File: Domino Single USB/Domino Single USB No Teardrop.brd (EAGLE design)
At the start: 25.4 x 33 mm, 22 parts, among them J1 MH10-1, J2 USB_AF-006, J3 MH10-1

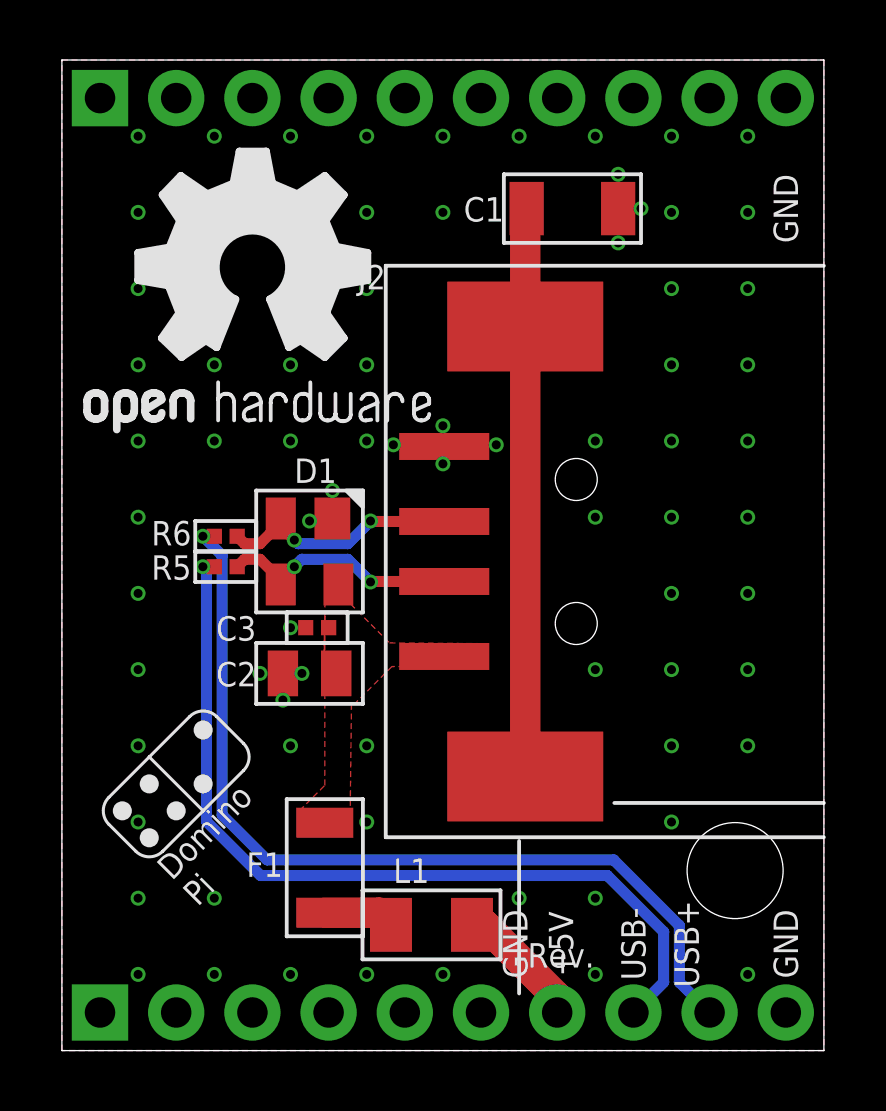
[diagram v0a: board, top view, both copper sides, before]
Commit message: Re-routed Single USB tile to remove vias on USB traces
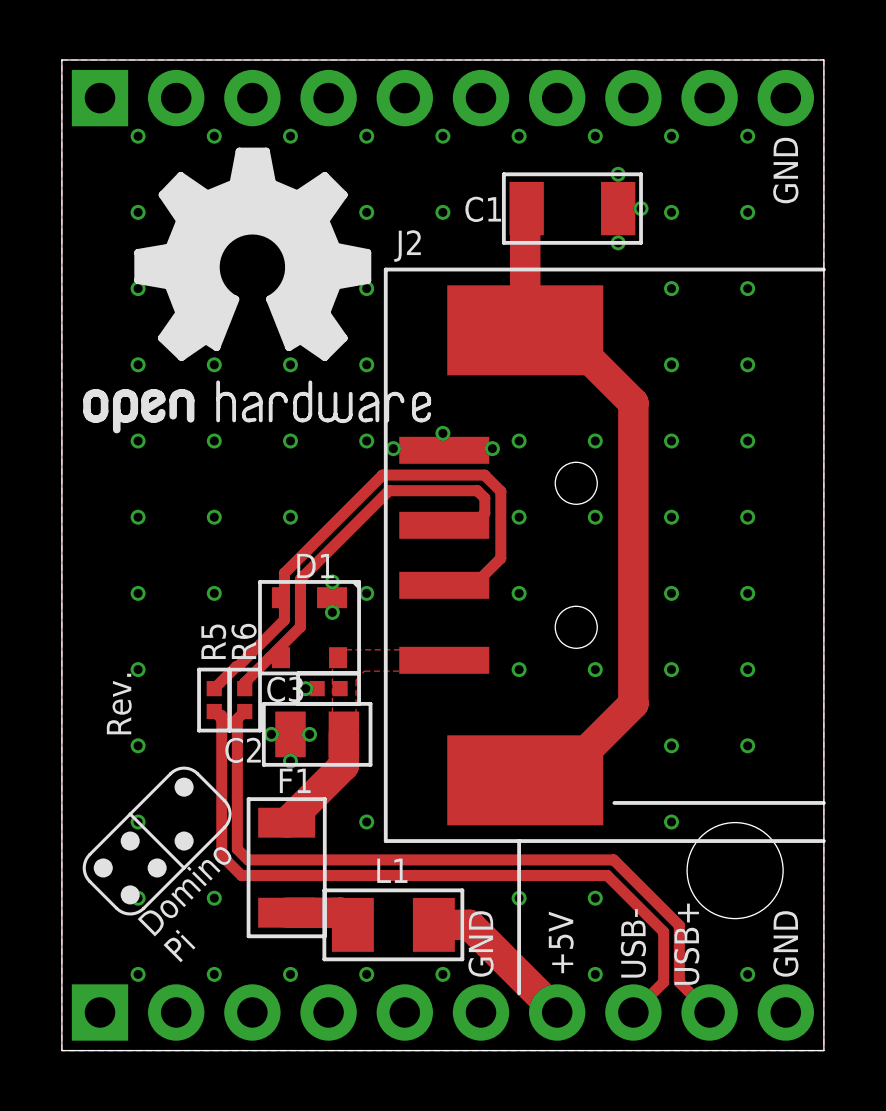
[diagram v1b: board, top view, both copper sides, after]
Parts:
- moved R6 5.50 mm to (6.10, 11.7), turned to 270 degrees
- moved R5 4.46 mm to (5.08, 11.7), turned to 270 degrees
- moved D1 2.54 mm to (8.26, 14.1)
- moved C3 2.07 mm to (8.89, 12.1)
- moved C2 2.05 mm to (8.51, 10.5)
- moved U$10 2.01 mm to (3.17, 6.99)
- moved L1 1.27 mm to (11.0, 4.19)
- moved F1 1.27 mm to (7.49, 6.10)
- moved J2 0.13 mm to (17.1, 16.5)
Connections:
- net D_N: now also D1.2; no longer D1.3
- net D_P: now also D1.3; no longer D1.2
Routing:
- net D_N: track 8.19 -> 18.3 mm, vias 2 -> 0
- net USB_P: track 30.0 -> 23.8 mm, vias 1 -> 0
- net D_P: track 8.07 -> 14.3 mm, vias 2 -> 0
- net USB_N: track 28.8 -> 23.9 mm, vias 1 -> 0
- net PE: track 19.0 -> 23.5 mm
- net VBUS: track 0.00 -> 3.73 mm
- net +5V: track 4.35 -> 5.32 mm

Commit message: Domino Single USB Rev. C: changed Logos
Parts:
- removed U$13: (no value), Domino:OPEN_HARDWARE_LOGO
- added U$7: DOMINO_LOGO, Domino:DOMINO_LOGO
- moved U$11 11.4 mm to (14.0, 6.35)
- moved U$10 10.8 mm to (3.81, 17.8), turned to 90 degrees
- moved U$4 9.52 mm to (22.9, 16.5)
- moved U$8 1.27 mm to (5.71, 3.81)
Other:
- board text removed: "Domino Core"
- board text removed: "Domino Pi"
- board text removed: "Domino Qi"

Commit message: Domino Single USB Rev. C: removed the resetable fuse that causes too much drop for high-current USB devices
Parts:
- removed F1: 0ZCA0050FF2G, Domino:PTC1206
- moved L1 2.52 mm to (9.40, 6.10), turned to 90 degrees
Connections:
- removed net VPROT: F1.1, L1.2
- net VBUS: now also L1.2; no longer F1.2
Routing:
- net +5V: track 5.32 -> 8.55 mm
- net VPROT: track 2.37 -> 0.00 mm
- net VBUS: track 3.73 -> 3.10 mm
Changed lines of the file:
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@@
 <layer number="143" name="mvRestrict" color="7" fill="1" visible="no" active="no"/>
 <layer number="144" name="DrillLegend" color="7" fill="1" visible="yes" active="yes"/>
-<layer number="145" name="DrillLegend_01-16" color="2" fill="9" visible="no" active="yes"/>
-<layer number="146" name="DrillLegend_01-20" color="3" fill="9" visible="no" active="yes"/>
+<layer number="145" name="DrillLegend_01-16" color="2" fill="9" visible="yes" active="yes"/>
+<layer number="146" name="DrillLegend_01-20" color="3" fill="9" visible="yes" active="yes"/>
 <layer number="147" name="mMeasures" color="7" fill="1" visible="no" active="no"/>
 <layer number="148" name="mDocument" color="7" fill="1" visible="no" active="no"/>
@@
 <wire x1="20.32" y1="8.128" x2="20.32" y2="7.112" width="0.1016" layer="145"/>
 <wire x1="19.812" y1="7.62" x2="20.828" y2="7.62" width="0.1016" layer="145"/>
-<wire x1="10.16" y1="8.128" x2="10.16" y2="7.112" width="0.1016" layer="145"/>
-<wire x1="9.652" y1="7.62" x2="10.668" y2="7.62" width="0.1016" layer="145"/>
+<wire x1="10.795" y1="8.128" x2="10.795" y2="7.112" width="0.1016" layer="145"/>
+<wire x1="10.287" y1="7.62" x2="11.303" y2="7.62" width="0.1016" layer="145"/>
 <wire x1="2.54" y1="8.128" x2="2.54" y2="7.112" width="0.1016" layer="145"/>
 <wire x1="2.032" y1="7.62" x2="3.048" y2="7.62" width="0.1016" layer="145"/>
@@
 </plain>
 <attributes>
-<attribute name="DATE" value="20141230"/>
+<attribute name="DATE" value="20141231"/>
 <attribute name="DRAWN" value="M.STEMPIN"/>
 <attribute name="REV" value="C"/>
@@
 <attribute name="VALUE" x="8.89" y="12.065" size="0.8128" layer="27" rot="R180" align="center"/>
 </element>
-<element name="L1" library="Domino" package="FB1206" value="BLM31PG601SN1L" x="11.049" y="4.191" smashed="yes" rot="R180">
-<attribute name="SIZE" value="1206" x="30.099" y="-9.779" size="1.27" layer="27" rot="R180" display="off"/>
-<attribute name="PARTNO" value="BLM31PG601SN1L" x="30.099" y="-9.779" size="1.27" layer="27" rot="R180" display="off"/>
-<attribute name="OPT" value="600R/1A5" x="30.099" y="-9.779" size="1.27" layer="27" rot="R180" display="off"/>
-<attribute name="NAME" x="10.414" y="5.588" size="0.8128" layer="25" ratio="12"/>
-<attribute name="VALUE" x="11.049" y="4.191" size="0.8128" layer="27" ratio="12" rot="R180" align="center"/>
+<element name="L1" library="Domino" package="FB1206" value="BLM31PG601SN1L" x="9.398" y="6.096" smashed="yes" rot="R90">
+<attribute name="SIZE" value="1206" x="-4.572" y="-12.954" size="1.27" layer="27" rot="R90" display="off"/>
+<attribute name="PARTNO" value="BLM31PG601SN1L" x="-4.572" y="-12.954" size="1.27" layer="27" rot="R90" display="off"/>
+<attribute name="OPT" value="600R/1A5" x="-4.572" y="-12.954" size="1.27" layer="27" rot="R90" display="off"/>
+<attribute name="NAME" x="10.668" y="5.588" size="0.8128" layer="25" ratio="12"/>
+<attribute name="VALUE" x="9.398" y="6.096" size="0.8128" layer="27" ratio="12" rot="R90" align="center"/>
 </element>
 <element name="C2" library="Domino" package="C0805" value="10u" x="8.509" y="10.541" smashed="yes" rot="R180">
@@
 <attribute name="VALUE" x="8.509" y="10.541" size="0.8128" layer="27" rot="R180" align="center"/>
 </element>
-<element name="F1" library="Domino" package="PTC1206" value="0ZCA0050FF2G" x="7.493" y="6.096" smashed="yes" rot="R90">
-<attribute name="PARTNO" value="0ZCG0110FF2C" x="7.493" y="-11.684" size="1.27" layer="27" rot="R90" display="off"/>
-<attribute name="VOLT" value="8V" x="7.493" y="6.096" size="1.778" layer="27" rot="R90" display="off"/>
-<attribute name="RATE" value="0.5A" x="7.493" y="6.096" size="1.778" layer="27" rot="R90" display="off"/>
-<attribute name="NAME" x="8.382" y="9.398" size="0.8128" layer="25" rot="R180"/>
-<attribute name="VALUE" x="7.493" y="6.096" size="0.8128" layer="27" rot="R90" align="center"/>
-</element>
 <element name="J2" library="Domino" package="USB_AF-006" value="USB_AF-006" x="17.145" y="16.51" smashed="yes" rot="R90">
 <attribute name="PARTNO" value="USB_AF-006" x="17.145" y="16.51" size="1.778" layer="27" rot="R90" display="off"/>
@@
 <element name="U$1" library="Domino" package="ROHS_LOGO" value="" x="22.86" y="21.59" rot="MR0"/>
 <element name="U$11" library="Domino" package="ESD_LOGO" value="" x="13.97" y="6.35" rot="MR0"/>
-<element name="DRILEGEND" library="drilegend" package="DRILEGEND" value="" x="81.534" y="59.944"/>
 <element name="U$7" library="Domino" package="DOMINO_LOGO" value="DOMINO_LOGO" x="-45.72" y="-48.26">
 <attribute name="BOM" value="EXCLUDE" x="-45.72" y="-48.26" size="1.27" layer="27" display="off"/>
@@
 <element name="U$4" library="Domino" package="DOMINO_LOGO_SMALL" value="" x="22.86" y="16.51" rot="MR0"/>
 <element name="U$10" library="Domino" package="DOMINO_LOGO_SMALL" value="" x="3.81" y="17.78" rot="R90"/>
+<element name="DRILEGEND" library="drilegend" package="DRILEGEND" value="" x="81.534" y="59.944"/>
 </elements>
 <signals>
@@
 <via x="22.86" y="10.16" extent="1-16" drill="0.3"/>
 <via x="20.32" y="7.62" extent="1-16" drill="0.3"/>
-<via x="10.16" y="7.62" extent="1-16" drill="0.3"/>
+<via x="10.795" y="7.62" extent="1-16" drill="0.3"/>
 <via x="2.54" y="7.62" extent="1-16" drill="0.3"/>
 <via x="2.54" y="5.08" extent="1-16" drill="0.3"/>
@@
 <contactref element="C2" pad="1"/>
 <contactref element="C3" pad="1"/>
-<contactref element="F1" pad="2"/>
 <contactref element="J2" pad="1"/>
-<wire x1="9.398" y1="10.541" x2="9.398" y2="9.501" width="1.016" layer="1"/>
-<wire x1="9.398" y1="9.501" x2="7.493" y2="7.596" width="1.016" layer="1"/>
 <polygon width="0.2032" layer="1" thermals="no">
 <vertex x="14.1478" y="13.3604"/>
@@
 <vertex x="14.1478" y="12.6492"/>
 </polygon>
+<contactref element="L1" pad="2"/>
+<wire x1="9.398" y1="10.541" x2="9.398" y2="7.446" width="1.016" layer="1"/>
 </signal>
 <signal name="PE">
@@
 <wire x1="15.445" y1="9.01" x2="16.503" y2="9.01" width="1.016" layer="1"/>
 </signal>
-<signal name="VPROT">
-<contactref element="L1" pad="2"/>
-<contactref element="F1" pad="1"/>
-<wire x1="7.493" y1="4.596" x2="9.294" y2="4.596" width="1.016" layer="1"/>
-<wire x1="9.294" y1="4.596" x2="9.699" y2="4.191" width="1.016" layer="1"/>
-</signal>
 <signal name="+5V">
 <contactref element="L1" pad="1"/>
 <contactref element="J1" pad="7"/>
-<wire x1="12.399" y1="4.191" x2="13.589" y2="4.191" width="1.016" layer="1"/>
 <wire x1="13.589" y1="4.191" x2="16.51" y2="1.27" width="1.016" layer="1"/>
+<wire x1="13.589" y1="4.191" x2="9.953" y2="4.191" width="1.016" layer="1"/>
+<wire x1="9.953" y1="4.191" x2="9.398" y2="4.746" width="1.016" layer="1"/>
 </signal>
 <signal name="USB_P" class="1">

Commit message: Added USB power switch to Sinfle USB tile
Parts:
- added C4: 10u, Domino:C0805
- added C5: 1n, Domino:C1206
- added R1: 100k, Domino:R0402
- added R2: 15k, Domino:R0402
- added U1: MP65151DJ, Domino:SOT23-6
- C1: value 1n -> 10u; device Domino:C1206 -> Domino:C0603
- C2: value 10u -> 220u; device Domino:C0805 -> Domino:C/6032-25
- J2: value USB_AF-006 -> MH10-1; device Domino:USB_AF-006 -> Domino:MH10-1-0.1
- J3: value MH10-1 -> USB_AF-006; device Domino:MH10-1-0.1 -> Domino:USB_AF-006
- moved J1 30.5 mm to (1.27, 31.8)
- moved J2 22.0 mm to (1.27, 1.27), flipped to the bottom, turned to 180 degrees
- moved J3 22.0 mm to (17.1, 16.5), flipped to the top, turned to 90 degrees
- moved C1 21.1 mm to (3.30, 12.1), turned to 180 degrees
- moved C2 7.41 mm to (2.16, 6.73), turned to 270 degrees
- moved U$10 1.17 mm to (2.67, 18.0)
- renumbered R5 to R3, R6 to R4, U$7 to S1
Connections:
- new net DP_PWR: C2.1, L1.1, U1.6
- new net ILIM: R2.1, U1.5
- new net JTAG_TDI: J1.3, R1.1, U1.3
- net +5V: now also C1.1, J2.7, R1.2, U1.1; no longer J1.7, L1.1
- net D_N: now also J3.2; no longer J2.2
- net D_P: now also J3.3; no longer J2.3
- net GND: now also C4.2, C5.2, J2.10, J2.6, J3.4, R2.2, U1.2; no longer J1.6, J2.4, J3.10
- net PE: now also C5.1, J3.S$1, J3.S$2; no longer C1.1, J2.S$1, J2.S$2
- net USB_N: now also J2.8; no longer J1.8
- net USB_P: now also J2.9; no longer J1.9
- net VBUS: now also C4.1, J3.1; no longer C2.1, J2.1
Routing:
- net +5V: track 8.55 -> 28.2 mm, vias 0 -> 2
- net JTAG_TDI: track 0.00 -> 17.3 mm
- net DP_PWR: track 0.00 -> 16.5 mm
- net ILIM: track 0.00 -> 3.44 mm
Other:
- board text added: "JTAG_TDI"
- board text added: "© 2014-2015, The Domino Team. All rights reserved."
- board text removed: "© 2014, The Domino Team. All rights reserved."

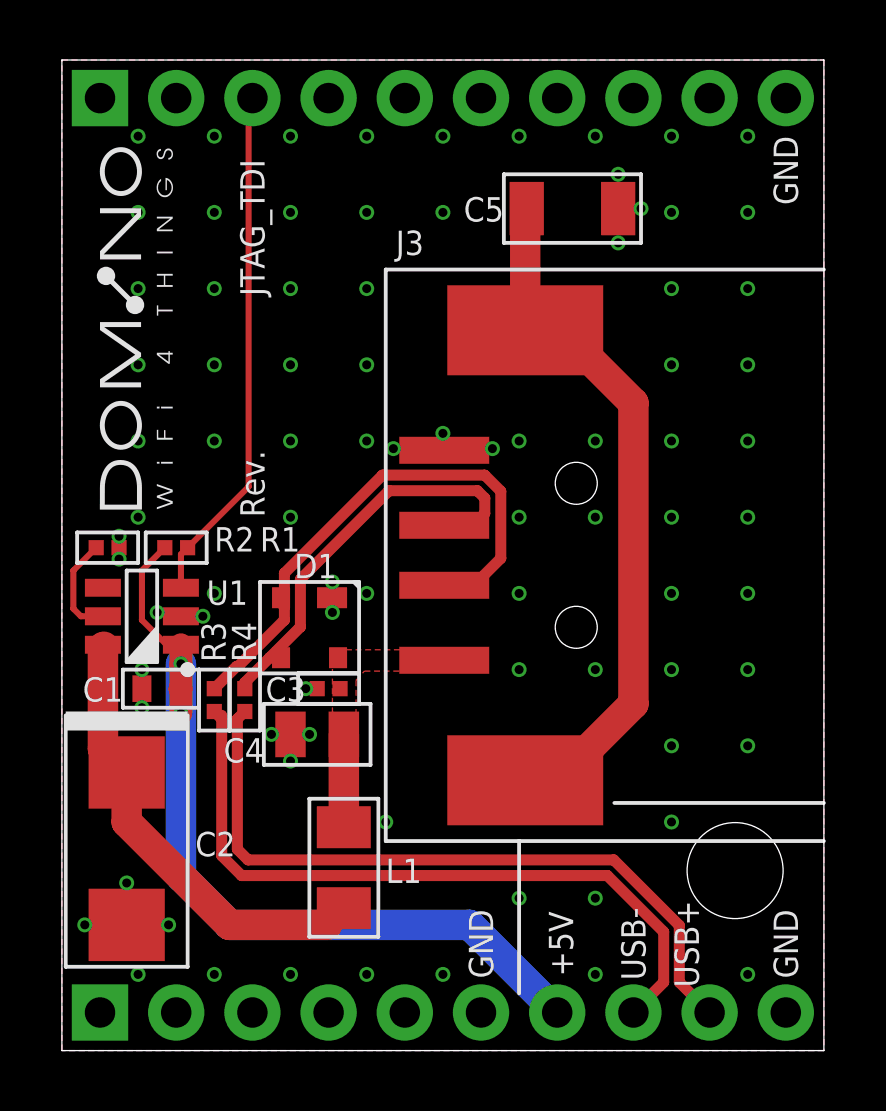
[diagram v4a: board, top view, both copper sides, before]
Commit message: Domino Single USB tile Rev. D: added resistors en power siwtch feedback and enable, changed output capacitor to smaller one
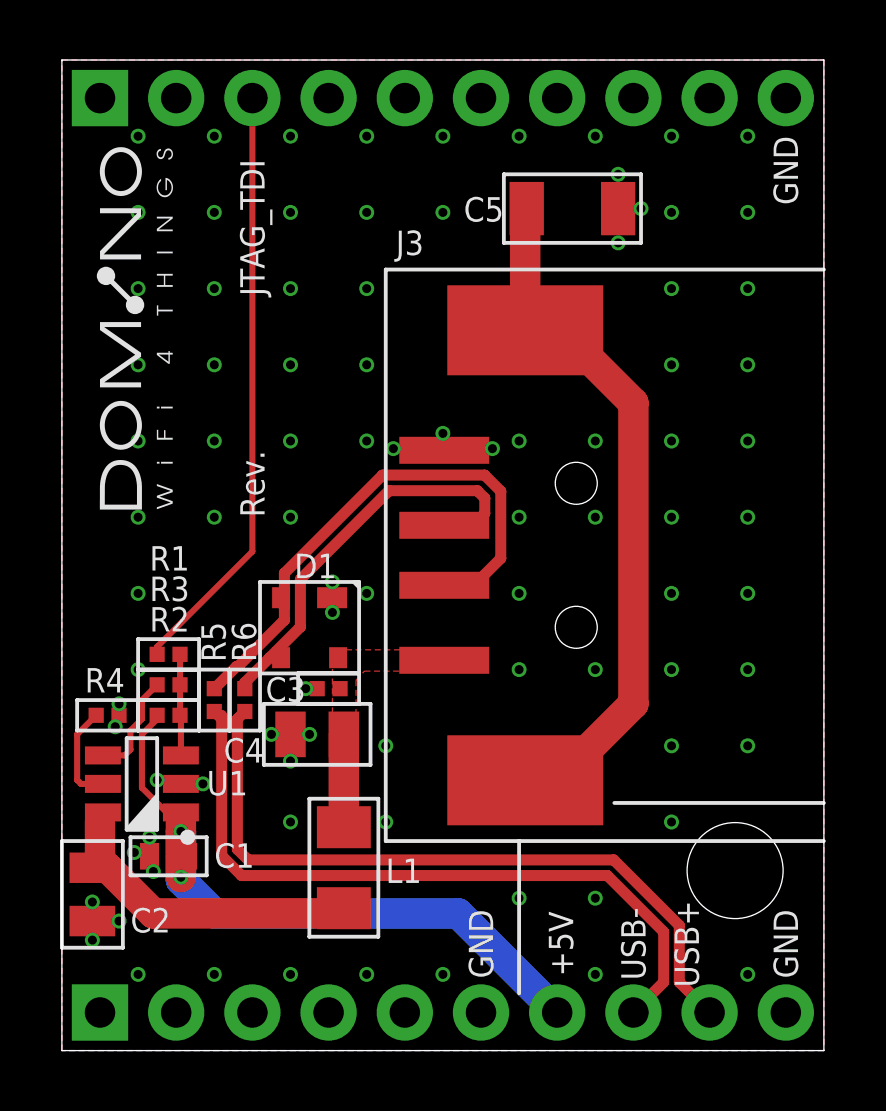
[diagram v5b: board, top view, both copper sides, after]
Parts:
- added R5, R6: 0R, Domino:R0402
- C2: value 220u -> 22u; device Domino:C/6032-25 -> Domino:C0805
- R1: value 100k -> 33R
- R2: value 15k -> 100k
- R4: value 0R -> 15k
- moved R2 5.95 mm to (3.56, 11.2), turned to 180 degrees
- moved C1 5.59 mm to (3.56, 6.48)
- moved U1 5.59 mm to (2.67, 8.89)
- moved R4 4.60 mm to (1.52, 11.2), turned to 0 degrees
- moved R1 3.57 mm to (3.56, 13.2)
- moved C2 1.91 mm to (1.02, 5.21)
- moved R3 1.61 mm to (3.56, 12.2), turned to 0 degrees
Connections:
- new net EN: R1.1, R2.1, R3.2, U1.3
- new net N$1: R3.1, U1.4
- net +5V: now also R2.2; no longer R1.2
- net D_N: now also R5.1; no longer R3.1
- net D_P: now also R6.1; no longer R4.1
- net GND: now also R4.2; no longer R2.2
- net ILIM: now also R4.1; no longer R2.1
- net JTAG_TDI: now also R1.2; no longer R1.1, U1.3
- net USB_N: now also R5.2; no longer R3.2
- net USB_P: now also R6.2; no longer R4.2
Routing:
- net +5V: track 28.2 -> 22.7 mm
- net DP_PWR: track 16.5 -> 11.1 mm
- net N$1: track 0.00 -> 3.53 mm
- net EN: track 0.00 -> 3.38 mm
- net JTAG_TDI: track 17.3 -> 19.9 mm
